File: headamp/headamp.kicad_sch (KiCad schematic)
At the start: 20 parts, among them SW2 S2 wokal, T1 OPT SE 5k:80R (>=25H, 45mA), U1 ECC82, U2 EL84 (trioda)

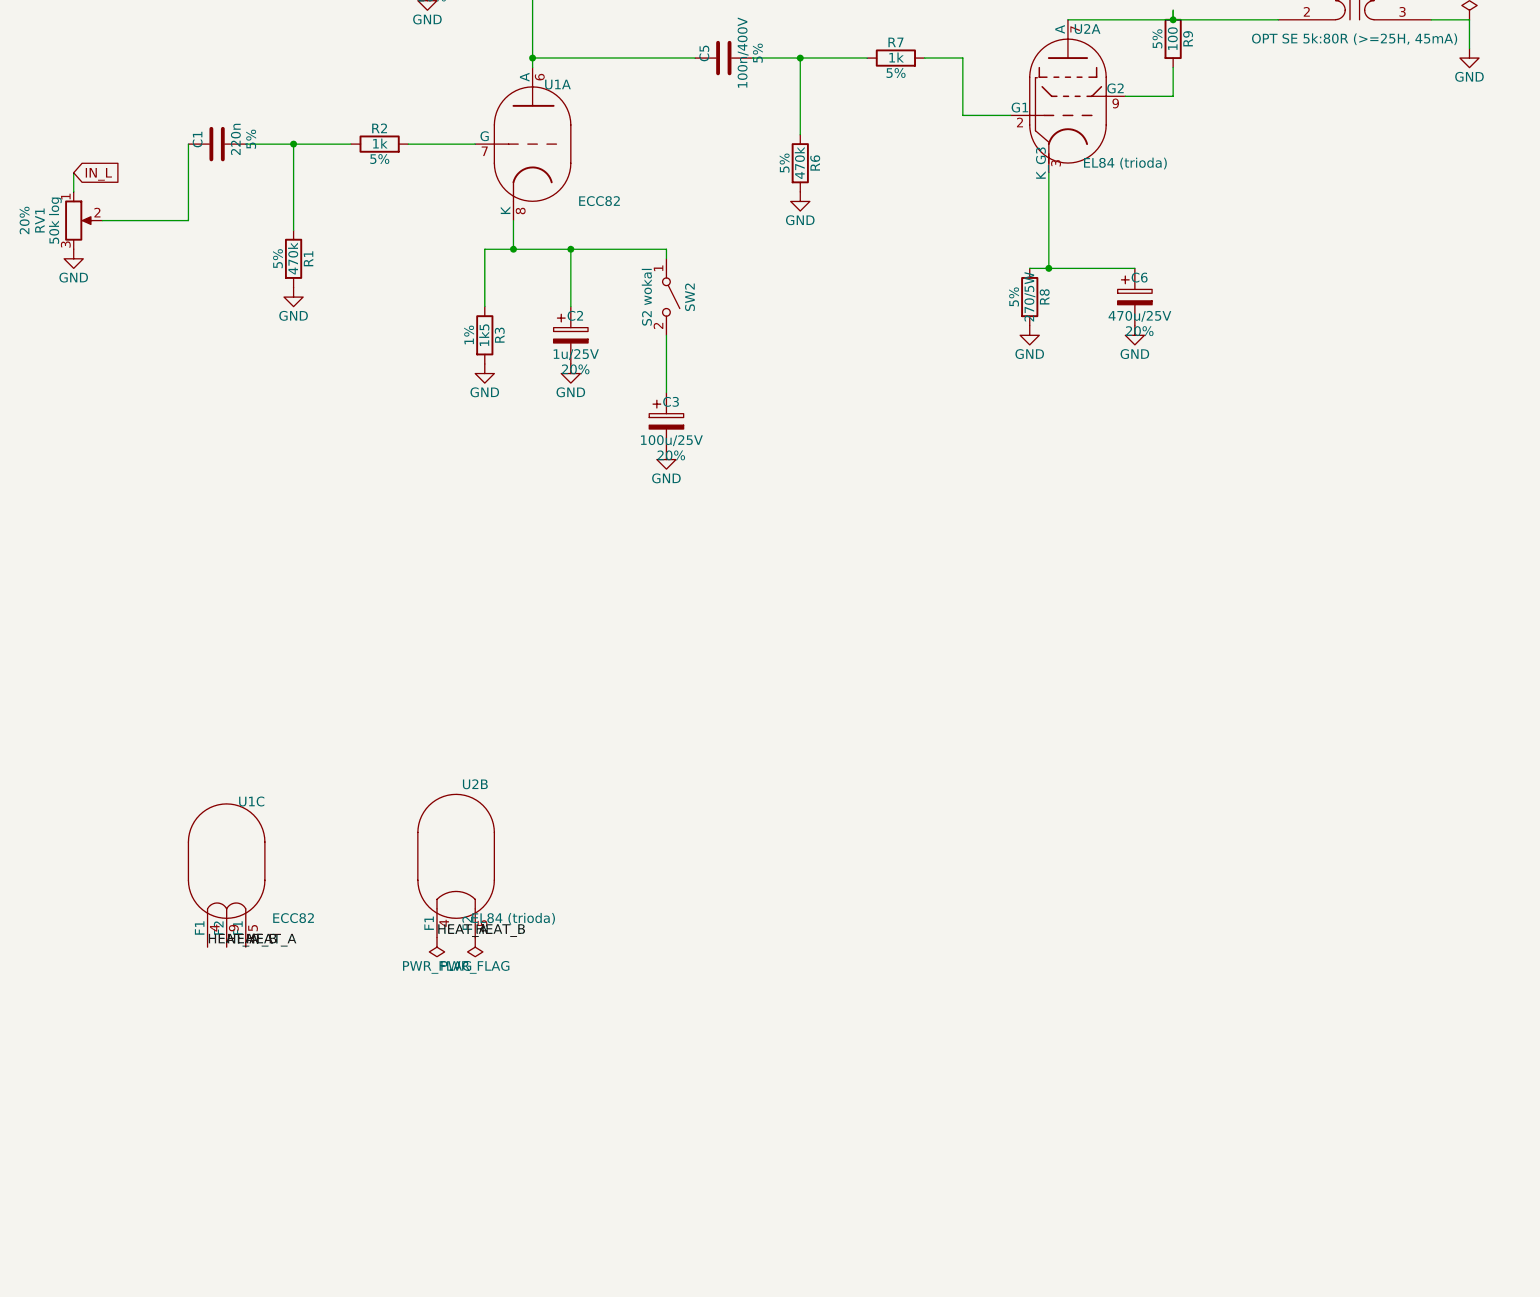
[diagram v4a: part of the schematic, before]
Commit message: headamp: kanal P (unit B ECC82 + drugi EL84 + drugi OPT + RV1 dual)
Kanal prawy dodany jako parametryzowana funkcja chan() w gen.py -
identyczna geometria kanalu L, przesunieta o 105,41 mm w Y (siatka
1,27mm), refy +200 (R201-R209/C201-C206/SW202/T201/U202), U1 unit B
(driver, ta sama lampa ECC82). RV1 zmieniony na potencjometr podwojny
(Device:R_Potentiometer_Dual_Separate) - unit1=L, unit2=P (DECYZJA,
brak wczesniejszej w docs). Etykiety IN_R/OUT_R, wspolne HEAT_A/HEAT_B
dla 3 lamp. check.py: funkcja chan() parametryzowana referencjami dla
L i P + asercje IN_L!=IN_R, OUT_L!=OUT_R. check.py OK (31 sieci), ERC
0 bledow / 4 oczekiwane ostrzezenia (wiszace IN_L/IN_R/OUT_L/OUT_R).

Co-Authored-By: Claude Sonnet 5 <noreply@anthropic.com>
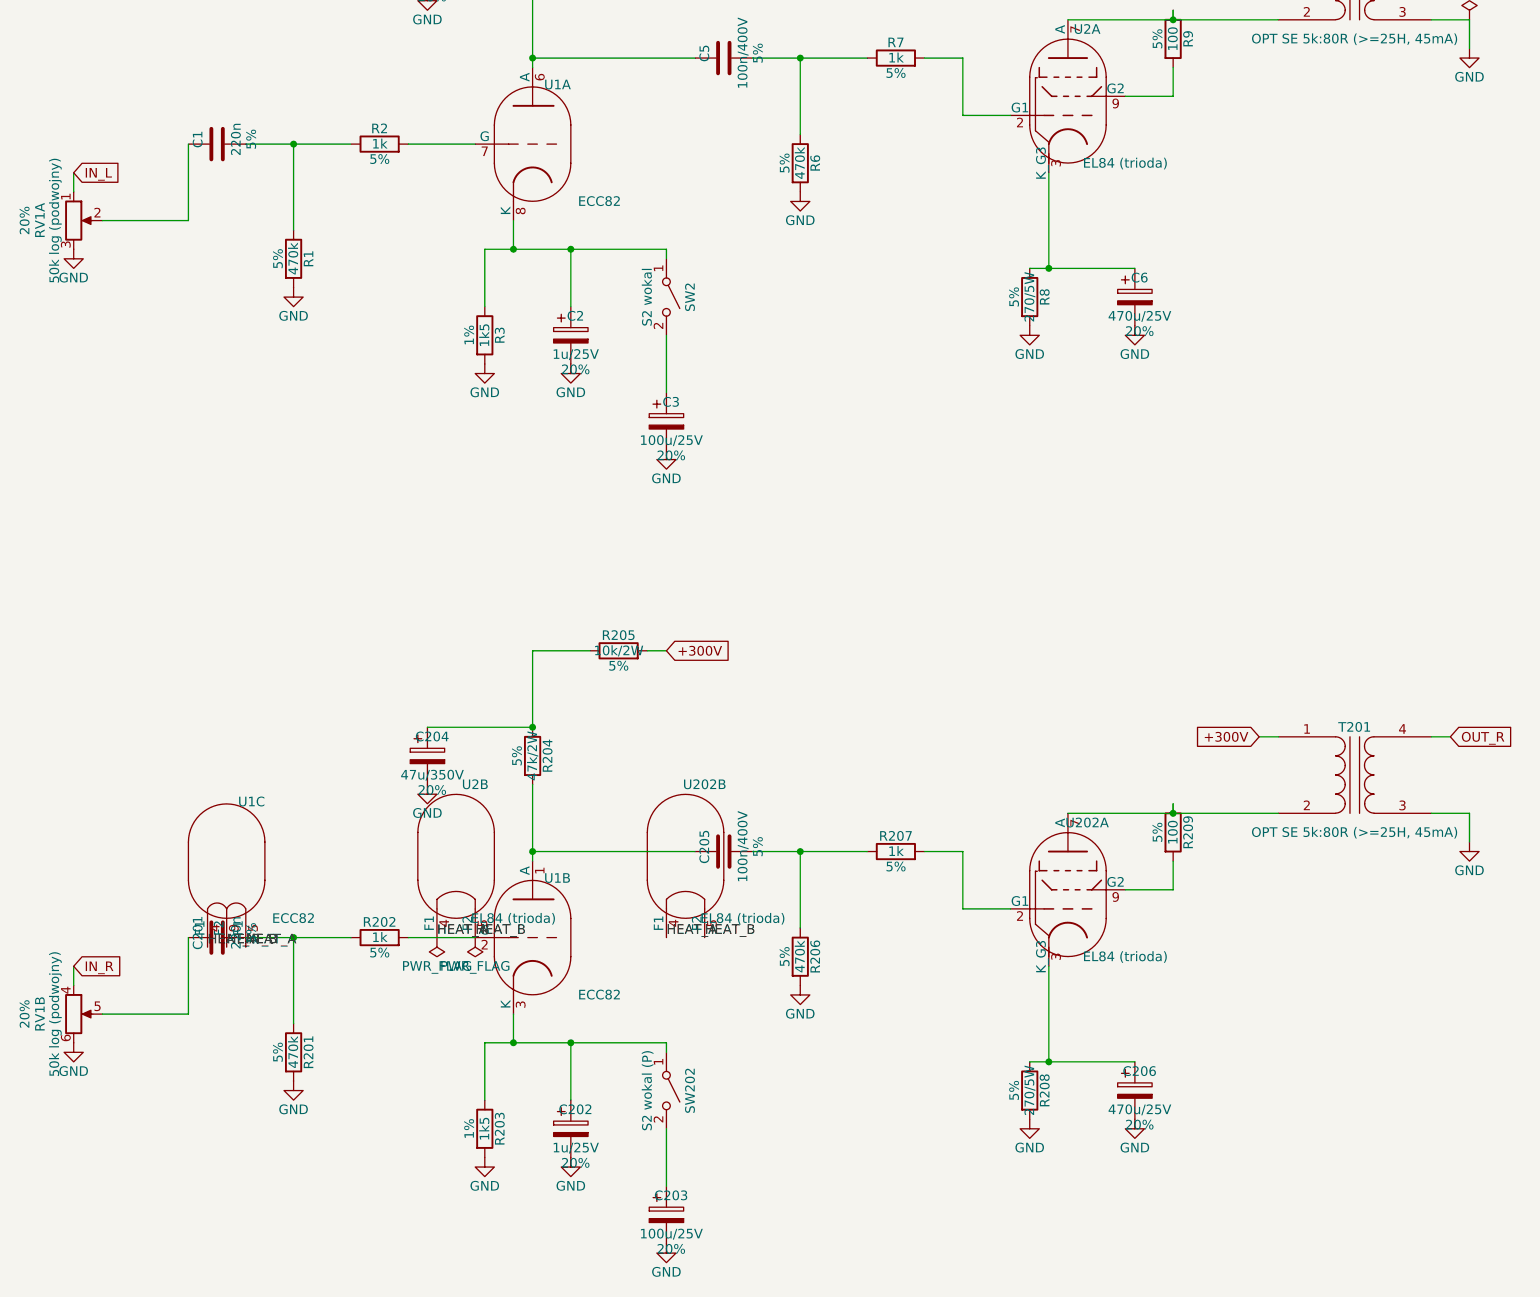
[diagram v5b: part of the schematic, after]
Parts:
- added C201: 220n, symbol Device:C
- added C202: 1u/25V, symbol Device:C_Polarized
- added C203: 100u/25V, symbol Device:C_Polarized
- added C204: 47u/350V, symbol Device:C_Polarized
- added C205: 100n/400V, symbol Device:C
- added C206: 470u/25V, symbol Device:C_Polarized
- added R201, R206: 470k, symbol Device:R
- added R202, R207: 1k, symbol Device:R
- added R203: 1k5, symbol Device:R
- added R204: 47k/2W, symbol Device:R
- added R205: 10k/2W, symbol Device:R
- added R208: 270/5W, symbol Device:R
- added R209: 100, symbol Device:R
- added unit 2 of RV1
- added SW202: S2 wokal (P), symbol Switch:SW_SPST
- added T201: OPT SE 5k:80R (>=25H, 45mA), symbol Device:Transformer_1P_1S
- added unit 2 of U1
- added U202: EL84 (trioda), symbol Valve:EL84
- RV1: value 50k log -> 50k log (podwojny); symbol Device:R_Potentiometer -> Device:R_Potentiometer_Dual_Separate
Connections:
- net HEAT_B is gone; now on net HEAT_A: U1.9 (F2), U2.5 (F2)
- net +300V: now also R205.2, T201.1 (AA)
- net GND: now also C202.2, C203.2, C204.2, C206.2, R201.2, R203.2, R206.2, R208.2, RV1.6, T201.3 (SA)
- net HEAT_A: now also R202.2, U1.2 (G), U202.4 (F1), U202.5 (F2)
- new net: C201.1, RV1.5
- new net: R209.1, T201.2 (AB), U202.7 (A)
- new net: R209.2, U202.9 (G2)
- new net: C206.1, R208.1, U202.3 (K_G3)
- new net: C202.1, R203.1, SW202.1 (A), U1.3 (K)
- new net: C201.2, R201.1, R202.1
- new net: C205.2, R206.1, R207.1
- new net: R207.2, U202.2 (G1)
- new net: C204.1, R204.1, R205.1
- new net: C205.1, R204.2, U1.1 (A)
- new net: C203.1, SW202.2 (B)
- new net IN_R: RV1.4
- new net OUT_R: T201.4 (SB)

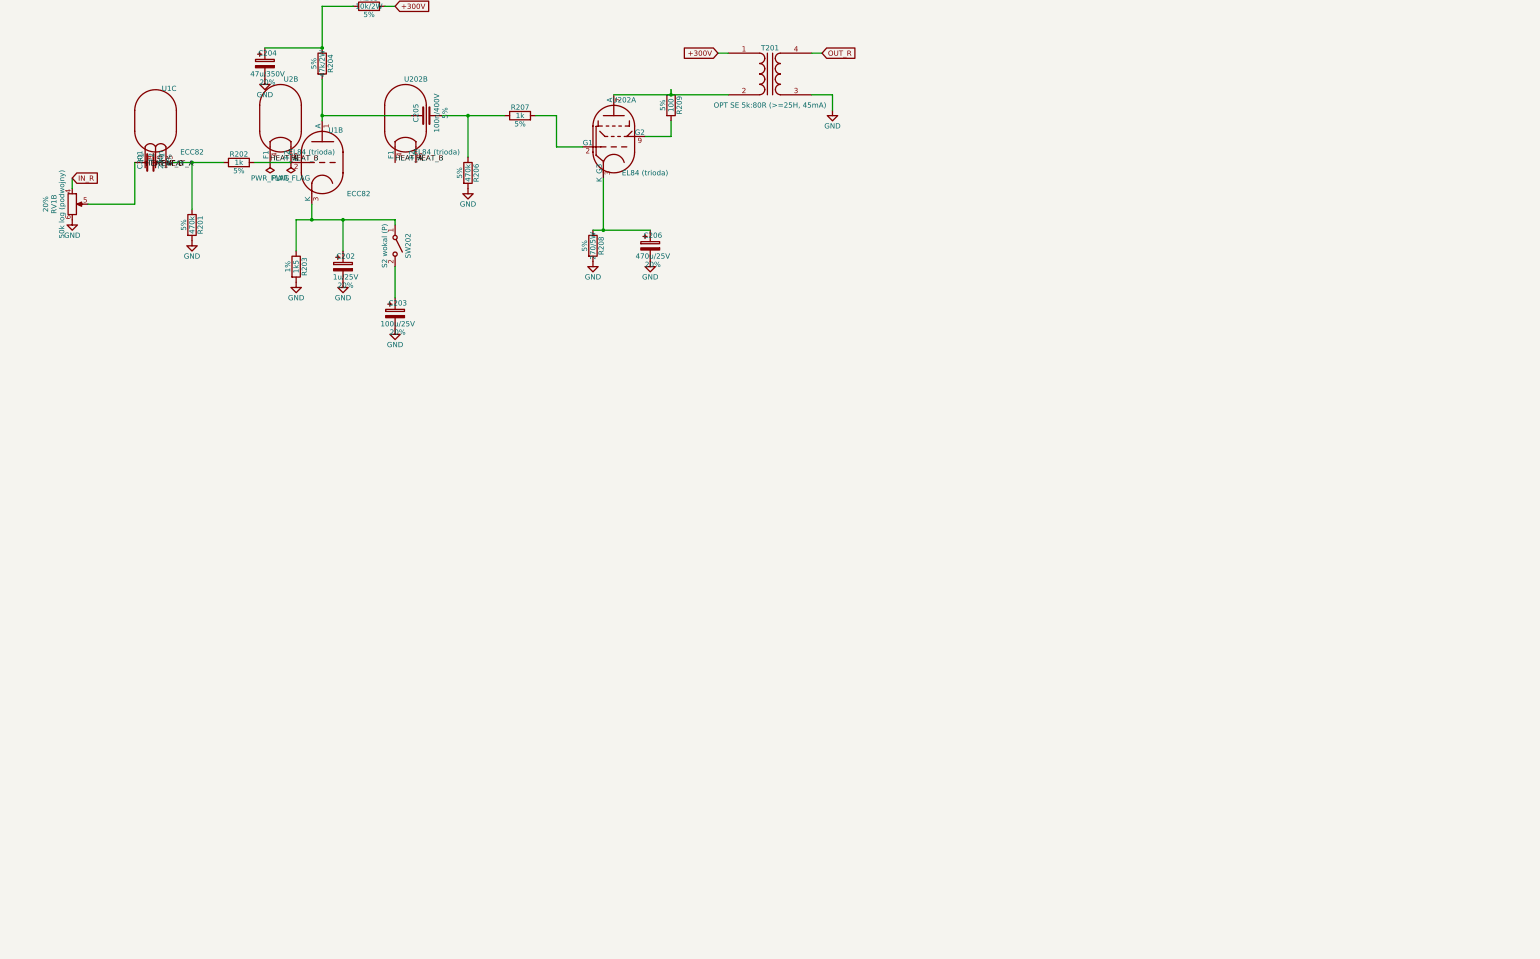
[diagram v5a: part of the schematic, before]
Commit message: headamp: zasilacz (B+ CLC, zarzenie LD1085, K1, ground breaker)
Sekcja zasilacza dodana na tym samym arkuszu, layout drutami (wzor
riaa/gen.py), numeracja 3xx + wyjatki nazwane (F1,SW1,J1,RT1,RV301,
NE1,T301,L1,K1,U301). Siec 230V (bezpiecznik, DPST, NTC, warystor +
neonowka) -> Transformer_1P_2S (230V:250V/0,15A+7V/3A) -> mostek
UF4007 + snubber -> CLC (220u/L1/220u) -> wspolny +300V (bez podzialu
per-kanal jak w RIAA) + bleeder 220k/2W. Elewacja 220k/47k + 10u ->
ELEV. Rozladowanie K1 + R306 4k7/10W (1:1 z common/riaa). Zarzenie
7V -> mostek 1N5822 -> 10000u (V_RAW) -> LD1085 -> 240R/976R -> 6,3V
DC (HEAT_A/HEAT_B, wspolne dla 3 lamp). Ground breaker 10R + 2x1N5408
+ 100n. Paper A3->A2 (DECYZJA, tresc ~427mm wysokosci).

check.py: asercje +300V/ELEV/HEAT_A/HEAT_B/V_RAW/GND/siec 230V/mostek/
zarzenie/ground breaker + diffy separacji L/N/PE/GND. check.py OK
(50 sieci). ERC 0 bledow, 5 oczekiwanych ostrzezen (wiszace IN/OUT x4,
multiple_net_names ELEV/HEAT_B - jak w common/riaa).

Co-Authored-By: Claude Sonnet 5 <noreply@anthropic.com>
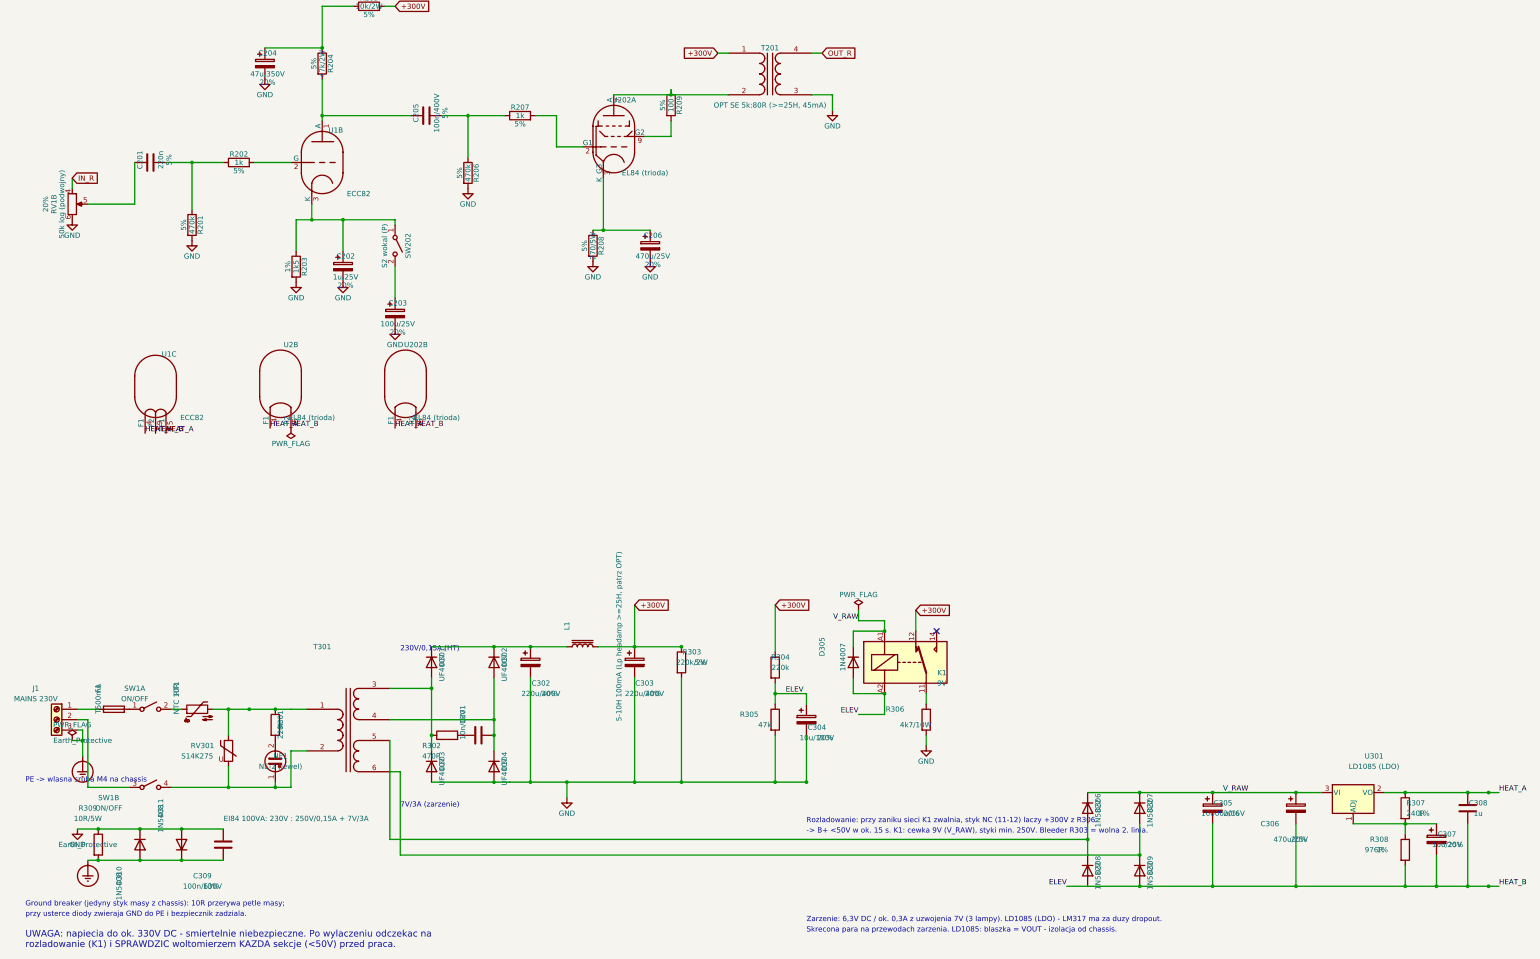
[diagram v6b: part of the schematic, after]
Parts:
- added C301: 10n/1kV, symbol Device:C
- added C302, C303: 220u/400V, symbol Device:C_Polarized
- added C304: 10u/100V, symbol Device:C_Polarized
- added C305: 10000u/16V, symbol Device:C_Polarized
- added C306: 470u/25V, symbol Device:C_Polarized
- added C307: 10u/25V, symbol Device:C_Polarized
- added C308: 1u, symbol Device:C
- added C309: 100n/630V, symbol Device:C
- added D301, D302, D303, D304: UF4007, symbol Device:D
- added D305: 1N4007, symbol Device:D
- added D306, D307, D308, D309: 1N5822, symbol Device:D
- added D310, D311: 1N5408, symbol Device:D
- added F1: T500mA, symbol Device:Fuse
- added J1: MAINS 230V, symbol Connector:Screw_Terminal_01x03
- added K1: 9V, symbol Relay:Relay_SPDT
- added L1: 5-10H 100mA (Lp headamp >=25H, patrz OPT), symbol Device:L_Iron
- added NE1: NE-2 (jewel), symbol Device:Lamp_Neon
- added R301, R304: 220k, symbol Device:R
- added R302: 470R, symbol Device:R
- added R303: 220k/2W, symbol Device:R
- added R305: 47k, symbol Device:R
- added R306: 4k7/10W, symbol Device:R
- added R307: 240R, symbol Device:R
- added R308: 976R, symbol Device:R
- added R309: 10R/5W, symbol Device:R
- added RT1: NTC 10R, symbol Device:Thermistor_NTC
- added RV301: S14K275, symbol Device:Varistor
- added SW1: ON/OFF, symbol Switch:SW_DPST_x2
- added T301: EI84 100VA: 230V : 250V/0,15A + 7V/3A, symbol Device:Transformer_1P_2S
- added U301: LD1085 (LDO), symbol Regulator_Linear:LM317_TO-220
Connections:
- net +300V: now also C303.1, K1.12, L1.2, R303.1, R304.1
- net GND: now also C302.2, C303.2, C304.2, C309.1, D303.2 (A), D304.2 (A), D310.1 (K), D311.2 (A), R303.2, R305.2, R306.2, R309.1
- net HEAT_A: now also C308.1, R307.1, U301.2 (VO); no longer R202.2, U1.2 (G), U1.9 (F2), U2.5 (F2), U202.5 (F2)
- new net: C302.1, D301.1 (K), D302.1 (K), L1.1
- new net: D301.2 (A), D303.1 (K), R302.1, T301.3 (SA)
- new net: K1.11, R306.1
- new net: C301.1, R302.2
- new net: C301.2, D302.2 (A), D304.1 (K), T301.4 (SB)
- new net: R301.1, RT1.2, RV301.1, T301.1 (AA)
- new net: NE1.1, RV301.2, SW1.4 (B), T301.2 (AB)
- new net: D307.2 (A), D309.1 (K), T301.6 (SD)
- new net: C307.1, R307.2, R308.1, U301.1 (ADJ)
- new net: J1.2 (Pin_2), SW1.3 (A)
- new net: NE1.2, R301.2
- new net: F1.1, J1.1 (Pin_1)
- new net: F1.2, SW1.1 (A)
- new net: D306.2 (A), D308.1 (K), T301.5 (SC)
- new net: RT1.1, SW1.2 (B)
- new net: R202.2, U1.2 (G)
- new net ELEV: C304.1, C305.2, C306.2, C307.2, C308.2, D305.2 (A), D308.2 (A), D309.2 (A), K1.A2, R304.2, R305.1, R308.2, U1.9 (F2), U2.5 (F2), U202.5 (F2)
- new net Earth_Protective: C309.2, D310.2 (A), D311.1 (K), J1.3 (Pin_3), R309.2
- new net V_RAW: C305.1, C306.1, D305.1 (K), D306.1 (K), D307.1 (K), K1.A1, U301.3 (VI)
- no-connect marks 0 -> 1
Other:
- note added: "-> B+ <50V w ok. 15 s. K1: cewka 9V (V_RAW), styki min. 250V. Bleeder R303 = wolna 2. linia."
- note added: "230V/0,15A (HT)"
- note added: "7V/3A (zarzenie)"
- note added: "Ground breaker (jedyny styk masy z chassis): 10R przerywa petle masy;"
- note added: "PE -> wlasna sruba M4 na chassis"
- note added: "Rozladowanie: przy zaniku sieci K1 zwalnia, styk NC (11-12) laczy +300V z R306"
- note added: "Skrecona para na przewodach zarzenia. LD1085: blaszka = VOUT - izolacja od chassis."
- note added: "UWAGA: napiecia do ok. 330V DC - smiertelnie niebezpieczne. Po wylaczeniu odczekac na"
- note added: "Zarzenie: 6,3V DC / ok. 0,3A z uzwojenia 7V (3 lampy). LD1085 (LDO) - LM317 ma za duzy dropout."
- note added: "przy usterce diody zwieraja GND do PE i bezpiecznik zadziala."
- note added: "rozladowanie (K1) i SPRAWDZIC woltomierzem KAZDA sekcje (<50V) przed praca."
- moved on the sheet: U1C, U202B, U2B
